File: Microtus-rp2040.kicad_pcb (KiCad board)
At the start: 2 copper layers, 69 x 50.5 mm, 36 parts, among them J1 Conn_01x04, J2 USB_C_Receptacle_USB2.0, SW1 SW_Push, SW3 SW_Push, SW4 SW_SPST, SW5 Rotary_Encoder, U1 AMS1117-3.3, U2 W25Q128JVS, U3 USBLC6-2SC6, U4 RP2040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

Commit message: moving things around
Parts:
- JP1: moved to B.Cu
- moved SW5 1.26 mm to (16.0, 16.8)
- turned JP1 to 0 degrees
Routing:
- net ENC_A: track 32.1 -> 33.4 mm
- net GND: track 59.2 -> 60.4 mm
- net ENC_B: track 38.5 -> 39.5 mm

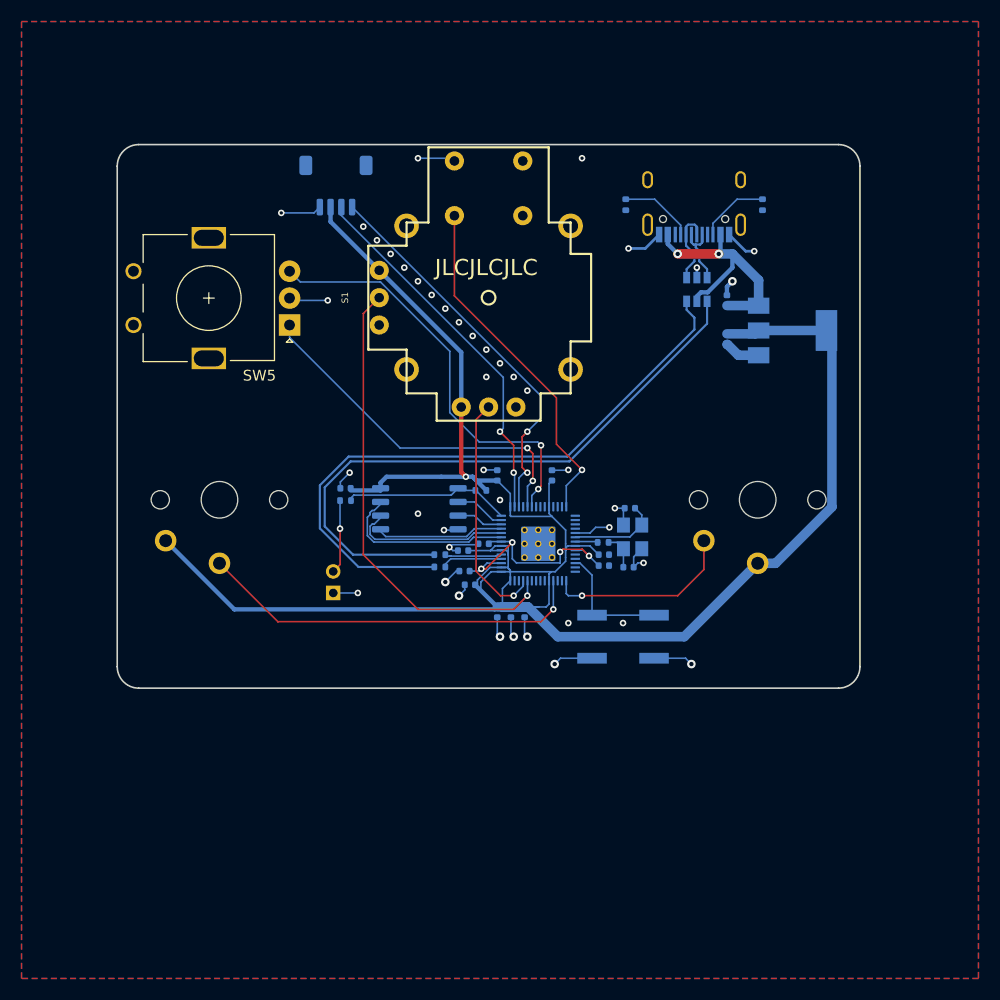
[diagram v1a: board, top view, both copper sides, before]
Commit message: add SWD and switch to KiCad 6
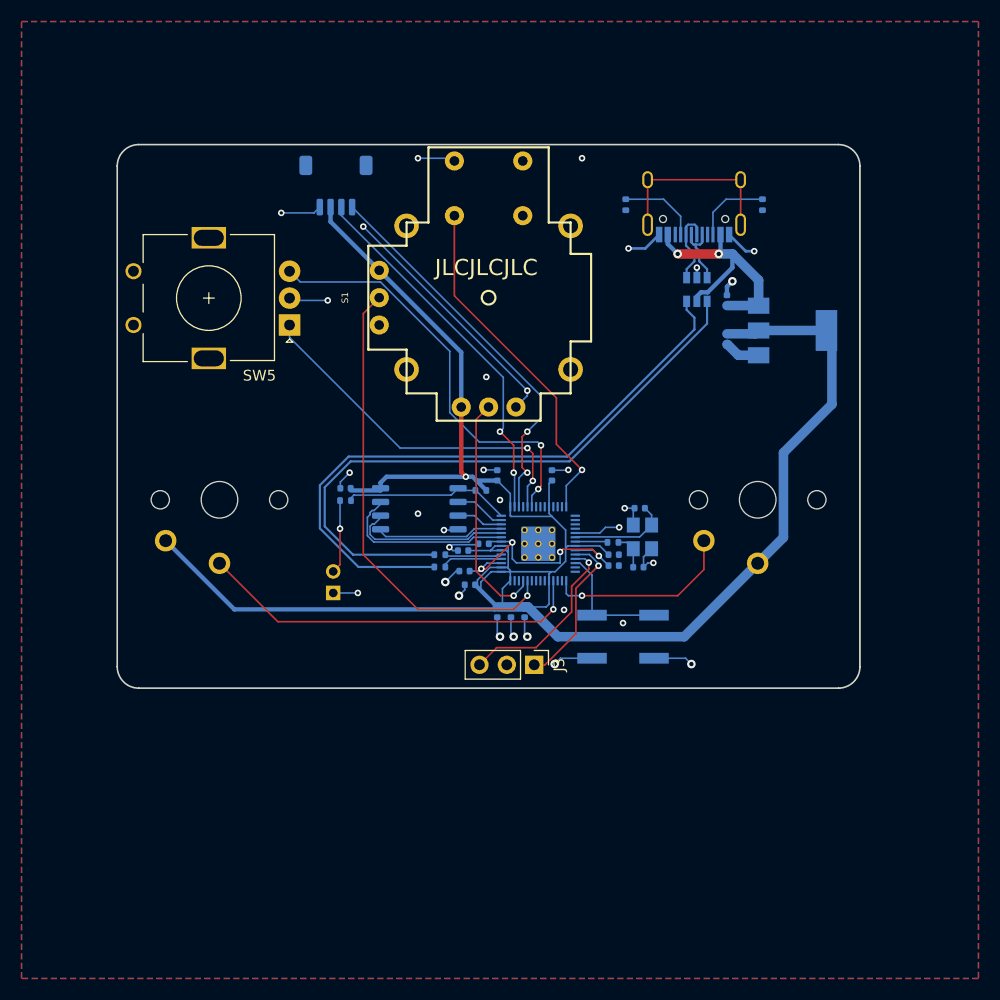
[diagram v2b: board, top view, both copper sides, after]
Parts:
- added J3: Conn_01x03, Connector_PinHeader_2.54mm:PinHeader_1x03_P2.54mm_Vertical, F.Cu at (38.7, 48.3)
- moved C16 0.91 mm to (46.1, 38.1)
- moved C4 0.91 mm to (48.5, 33.8)
- moved C5 0.91 mm to (48.4, 39.3)
- moved C7 0.91 mm to (46.1, 39.1)
- moved R5 0.91 mm to (46.1, 37.0)
- moved Y1 0.91 mm to (48.8, 36.4)
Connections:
- J2 pad A8: (no net) -> unconnected-(J2-PadA8)
- J2 pad B8: (no net) -> unconnected-(J2-PadB8)
- J2 pad S1: (no net) -> unconnected-(J2-PadS1)
- U4 pad 11: (no net) -> unconnected-(U4-Pad11)
- U4 pad 12: (no net) -> unconnected-(U4-Pad12)
- U4 pad 13: (no net) -> unconnected-(U4-Pad13)
- U4 pad 15: (no net) -> unconnected-(U4-Pad15)
- U4 pad 16: (no net) -> unconnected-(U4-Pad16)
- U4 pad 17: (no net) -> unconnected-(U4-Pad17)
- U4 pad 18: (no net) -> unconnected-(U4-Pad18)
- U4 pad 24: (no net) -> /SWCLK
- U4 pad 25: (no net) -> /SWD
- U4 pad 27: (no net) -> unconnected-(U4-Pad27)
- U4 pad 28: (no net) -> unconnected-(U4-Pad28)
- U4 pad 30: (no net) -> unconnected-(U4-Pad30)
- U4 pad 31: (no net) -> unconnected-(U4-Pad31)
- U4 pad 34: (no net) -> unconnected-(U4-Pad34)
- U4 pad 35: (no net) -> unconnected-(U4-Pad35)
- U4 pad 36: (no net) -> unconnected-(U4-Pad36)
- U4 pad 37: (no net) -> unconnected-(U4-Pad37)
- U4 pad 4: (no net) -> unconnected-(U4-Pad4)
- U4 pad 40: (no net) -> unconnected-(U4-Pad40)
- U4 pad 41: (no net) -> unconnected-(U4-Pad41)
- U4 pad 7: (no net) -> unconnected-(U4-Pad7)
- U4 pad 8: (no net) -> unconnected-(U4-Pad8)
- U4 pad 9: (no net) -> unconnected-(U4-Pad9)
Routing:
- net GND: track 60.4 -> 83.7 mm, vias 42 -> 31
- net /SWD: track 0.00 -> 17.2 mm, vias 0 -> 1
- net unconnected-(J2-PadS1): track 0.00 -> 17.0 mm
- net /SWCLK: track 0.00 -> 15.0 mm, vias 0 -> 1
- net +3V3: track 200.4 -> 194.9 mm
- net +1V1: track 22.4 -> 24.2 mm
- net /XIN: track 8.47 -> 9.35 mm
- net /XOUT: track 2.31 -> 3.02 mm
- net Net-(J2-PadB5): track 6.57 -> 7.17 mm
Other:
- net class Default removed
- board text added: "CLK GND SWD"

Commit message: Generate production files
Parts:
- C1, C2: footprint Capacitor_SMD:C_0402_1005Metric -> Capacitor_SMD:C_0603_1608Metric
- R1: value 1K -> 1k
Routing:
- net GND: track 83.7 -> 80.3 mm, vias 31 -> 32
